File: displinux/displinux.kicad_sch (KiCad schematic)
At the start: 168 parts, among them J10 USB4105-GF-A, J11 Conn_02x03_Odd_Even, J12 Conn_02x17_Odd_Even, J13 Conn_01x02, J15 HR911105A, J2 AudioJack4, J3 AudioJack4, J4 USB4105-GF-A, J5 Conn_01x04, J6 Conn_01x06, J7 Conn_01x40_MountingPin, J8 Conn_01x24_MountingPin, J9 Conn_01x03, U1 SY8089AAAC, U2 SY8089AAAC, U3 SY8089AAAC, U4 SY7201ABC, U5 F133, U6 XC6206PxxxMR, U7 W25N01KV, U8 DP83848C, X1 ASE-50MHz, Y1 24M, Y2 Crystal

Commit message: add schematic
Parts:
- removed C12, C34, C6: 10u, Capacitor_SMD:C_0603_1608Metric, symbol Device:C
- removed C16, C17, C18, C19, C20, C21, C22, C24, C25, C26, C27, C32, C33, C35, C37, C39, C9: 0.1u, Capacitor_SMD:C_0603_1608Metric, symbol Device:C
- removed C28: 33p, Capacitor_SMD:C_0603_1608Metric, symbol Device:C
- removed D10, D11, D12, D13, D4, D6, D7, D8, D9: ESD9B3.3ST5G, Diode_SMD:D_SOD-923, symbol Diode:ESD9B3.3ST5G
- removed D3: D, Diode_SMD:D_SOD-323, symbol Device:D
- removed H5: MountingHole_Pad, Connector_Wire:SolderWirePad_1x01_SMD_5x10mm, symbol Mechanical:MountingHole_Pad
- removed J11: Conn_02x03_Odd_Even, Connector_PinHeader_2.00mm:PinHeader_2x03_P2.00mm_Vertical, symbol Connector_Generic:Conn_02x03_Odd_Even
- removed J13: Conn_01x02, Connector_PinHeader_2.00mm:PinHeader_1x02_P2.00mm_Vertical, symbol Connector_Generic:Conn_01x02
- removed J3: AudioJack4, Connector_Audio:Jack_3.5mm_PJ320D_Horizontal, symbol XassetteAsterisk-rescue:AudioJack4-Connector
- removed J5: Conn_01x04, Connector_PinSocket_2.00mm:PinSocket_1x04_P2.00mm_Vertical, symbol Connector_Generic:Conn_01x04
- removed JP1, JP2, JP3: Jumper_3_Open, Jumper:SolderJumper-3_P2.0mm_Open_TrianglePad1.0x1.5mm, symbol XassetteAsterisk-rescue:Jumper_3_Open-Jumper
- removed L3: 2.2u, Inductor_SMD:L_Wuerth_MAPI-2510, symbol Device:L
- removed R15, R4: 100k, Resistor_SMD:R_0603_1608Metric, symbol Device:R
- removed R19: 10M, Resistor_SMD:R_0603_1608Metric, symbol Device:R
- removed R28, R29: 10k, Resistor_SMD:R_0603_1608Metric, symbol Device:R
- removed R7: 200k, Resistor_SMD:R_0603_1608Metric, symbol Device:R
- removed RN1, RN2: R_Pack04, Resistor_SMD:R_Array_Convex_4x0603, symbol Device:R_Pack04
- removed U2: SY8089AAAC, Package_TO_SOT_SMD:SOT-23-5, symbol XassetteAsterisk-rescue:SY8089AAAC-2021-10-05_14-05-45
- removed U7: W25N01KV, Package_SON:WSON-8-1EP_6x5mm_P1.27mm_EP3.4x4.3mm, symbol XassetteAsterisk-rescue:W25Q32JVSS-Memory_Flash
- added C42: 10u, Capacitor_SMD:C_0603_1608Metric, symbol Device:C
- added C43, C46, C51, C52, C55, C57, C58, C60, C61, C62, C63: 0.1u, Capacitor_SMD:C_0603_1608Metric, symbol Device:C
- added D2: LED, LED_SMD:LED_0603_1608Metric, symbol Device:LED
- added R38: 1k, Resistor_SMD:R_0603_1608Metric, symbol Device:R
- added R42, R43, R44: 2.2K, Resistor_SMD:R_0603_1608Metric, symbol Device:R
- added R45: 100k, Resistor_SMD:R_0603_1608Metric, symbol Device:R
- added R49, R50, R51, R52, R53, R54: 10k, Resistor_SMD:R_0603_1608Metric, symbol Device:R
- added U6: XC6206P_1_2_MR, Package_TO_SOT_SMD:SOT-23, symbol Regulator_Linear:XC6206PxxxMR
- added U8: W25N01KV, Package_SON:WSON-8-1EP_6x5mm_P1.27mm_EP3.4x4.3mm, symbol XassetteAsterisk-rescue:W25Q32JVSS-Memory_Flash
- C11: renamed from C63; footprint Capacitor_SMD:C_0805_2012Metric -> Capacitor_SMD:C_0603_1608Metric
- C20: renamed from C61; footprint Capacitor_SMD:C_0805_2012Metric -> Capacitor_SMD:C_0603_1608Metric
- C21: renamed from C62; footprint Capacitor_SMD:C_0805_2012Metric -> Capacitor_SMD:C_0603_1608Metric
- C22: renamed from C64; footprint Capacitor_SMD:C_0805_2012Metric -> Capacitor_SMD:C_0603_1608Metric
- C24: renamed from C67; footprint Capacitor_SMD:C_0805_2012Metric -> Capacitor_SMD:C_0603_1608Metric
- C25: renamed from C69; footprint Capacitor_SMD:C_0805_2012Metric -> Capacitor_SMD:C_0603_1608Metric
- C26: renamed from C70; footprint Capacitor_SMD:C_0805_2012Metric -> Capacitor_SMD:C_0603_1608Metric
- C47, C48: value 1u -> 0.1u
- C8: renamed from C66; footprint Capacitor_SMD:C_0805_2012Metric -> Capacitor_SMD:C_0603_1608Metric
- C9: renamed from C68; footprint Capacitor_SMD:C_0805_2012Metric -> Capacitor_SMD:C_0603_1608Metric
- J1: renamed from J4; footprint USB4105-GF-A:GCT_USB4105-GF-A -> Connector_USB:USB_C_Receptacle_G-Switch_GT-USB-7010ASV
- J2: renamed from J10; footprint USB4105-GF-A:GCT_USB4105-GF-A -> Connector_USB:USB_C_Receptacle_G-Switch_GT-USB-7010ASV
- L1: renamed from L2; footprint Inductor_SMD:L_Wuerth_MAPI-2510 -> Inductor_SMD_Wurth:L_Wurth_WE-LQSH-3012
- L2: renamed from L4; footprint Inductor_SMD:L_Wuerth_MAPI-2510 -> Inductor_SMD_Wurth:L_Wurth_WE-LQSH-3012
- L3: renamed from L1; footprint Inductor_SMD:L_Wuerth_MAPI-2510 -> Inductor_SMD_Wurth:L_Wurth_WE-LQSH-3012
- R13: renamed from R43; footprint Resistor_SMD:R_0805_2012Metric -> Resistor_SMD:R_0603_1608Metric
- R14: renamed from R44; footprint Resistor_SMD:R_0805_2012Metric -> Resistor_SMD:R_0603_1608Metric
- R15: renamed from R45; footprint Resistor_SMD:R_0805_2012Metric -> Resistor_SMD:R_0603_1608Metric
- R16: renamed from R46; footprint Resistor_SMD:R_0805_2012Metric -> Resistor_SMD:R_0603_1608Metric
- R18: value 2.2k -> 7.87k
- R19: renamed from R50; footprint Resistor_SMD:R_0805_2012Metric -> Resistor_SMD:R_0603_1608Metric
- R20: renamed from R38; footprint Resistor_SMD:R_0805_2012Metric -> Resistor_SMD:R_0603_1608Metric
- R21: renamed from R51; footprint Resistor_SMD:R_0805_2012Metric -> Resistor_SMD:R_0603_1608Metric
- R22: renamed from R35; footprint Resistor_SMD:R_0805_2012Metric -> Resistor_SMD:R_0603_1608Metric
- R23: renamed from R36; footprint Resistor_SMD:R_0805_2012Metric -> Resistor_SMD:R_0603_1608Metric
- R24: renamed from R40; footprint Resistor_SMD:R_0805_2012Metric -> Resistor_SMD:R_0603_1608Metric
- R26: renamed from R47; footprint Resistor_SMD:R_0805_2012Metric -> Resistor_SMD:R_0603_1608Metric
- R27: renamed from R39; footprint Resistor_SMD:R_0805_2012Metric -> Resistor_SMD:R_0603_1608Metric
- R28: renamed from R48; footprint Resistor_SMD:R_0805_2012Metric -> Resistor_SMD:R_0603_1608Metric
- R29: renamed from R49; footprint Resistor_SMD:R_0805_2012Metric -> Resistor_SMD:R_0603_1608Metric
- R32: renamed from R34; footprint Resistor_SMD:R_0805_2012Metric -> Resistor_SMD:R_0603_1608Metric
- U5: renamed from U6; value XC6206PxxxMR -> XC6206P_2_8_MR
- XS1: footprint usd:Conn_uSDcard -> Connector_Card:microSD_HC_Hirose_DM3AT-SF-PEJM5
- renumbered C52 to C1, C60 to C10, C43 to C12, C38 to C15, C11 to C16, C5 to C17, C8 to C18, C54 to C19, C58 to C2, C65 to C23, C55 to C27, C29 to C28, C3 to C29, C14 to C3, C23 to C30, C30 to C31, C13 to C32, C31 to C33, C7 to C34, C10 to C35, C53 to C36, C36 to C37, C46 to C38, C51 to C39, C44 to C4, C42 to C41, C57 to C44, C2 to C45, C41 to C5, C1 to C53, C4 to C54, C45 to C6, C15 to C7, D2 to D1, D5 to D3, D1 to D5, J2 to J3, J12 to J4, J15 to J5, J8 to J6, J6 to J7, J7 to J8, R21 to R1, R13 to R10, R17 to R11, R11 to R12, R14 to R17, R23 to R2, R1 to R25, R26 to R3, R3 to R30, R6 to R31, R22 to R33, R2 to R34, R31 to R35, R32 to R36, R5 to R39, R27 to R4, R8 to R40, R20 to R41, R9 to R46, R24 to R47, R25 to R48, R30 to R5, R33 to R6, R12 to R7, R16 to R8, R10 to R9, U8 to U1, U1 to U2, U5 to U3, U3 to U4, U4 to U7
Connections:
- net VCC_PD is gone; now on net +3V3: C36.2, U3.66 (VCC-PD)
- net VCC_PG is gone; now on net +3V3: C12.2, U3.128 (VCC-PG)
- net +1V8: now also C40.1, C59.1, U3.28 (LDOA-OUT), C57.1, C58.1, C60.1, C61.1, C62.1, C63.1; no longer R18.1
- net +3V3: now also C50.1, J4.4 (Pin_4), J6.11 (Pin_11), U3.34 (VCC-PE), C42.2, C51.1, C52.1, C55.1, R42.1, R43.1, R44.1, R45.1, R49.1, U6.3 (VI), U8.8 (VCC); no longer C40.1, C56.1
- net +5V: now also J4.3 (Pin_3), R18.1
- net CLKO: now also J4.23 (Pin_23); no longer J4.33 (Pin_33)
- net CSI-PWDN: now also J6.8 (Pin_8), R38.1; no longer J6.5 (Pin_5)
- net CSI-RST#: now also J6.6 (Pin_6); no longer J6.4 (Pin_4)
- net GND: now also C49.2, C50.2, J4.31 (Pin_31), J4.32 (Pin_32), J4.33 (Pin_33), J4.34 (Pin_34), J6.15 (Pin_15), J6.2 (Pin_2), C42.1, C43.2, C46.2, C51.2, C52.2, C55.2, C57.2, C58.2, C60.2, C61.2, C62.2, C63.2, D2.1 (K), R38.2, R49.2, R50.2, R51.2, R52.2, R53.2, R54.2, U6.1 (GND), U8.4 (GND); no longer J4.13 (Pin_13), J4.14 (Pin_14), J6.1 (Pin_1), J6.11 (Pin_11), J6.14 (Pin_14)
- net HPOUTFB: now also J4.7 (Pin_7)
- net HS_MIC: no longer R18.2
- net LCD0-D0: now also J8.21 (Pin_21), R53.1; no longer J8.5 (Pin_5)
- net LCD0-D1: now also J8.22 (Pin_22), R54.1; no longer J8.6 (Pin_6)
- net LCD0-D16: now also J8.5 (Pin_5); no longer J8.21 (Pin_21)
- net LCD0-D17: now also J8.6 (Pin_6), R50.1; no longer J8.22 (Pin_22)
- net LCD0-D18: now also J8.7 (Pin_7); no longer J8.23 (Pin_23)
- net LCD0-D19: now also J8.8 (Pin_8); no longer J8.24 (Pin_24)
- net LCD0-D2: now also J8.23 (Pin_23); no longer J8.7 (Pin_7)
- net LCD0-D20: now also J8.9 (Pin_9); no longer J8.25 (Pin_25)
- net LCD0-D21: now also J8.10 (Pin_10); no longer J8.26 (Pin_26)
- net LCD0-D22: now also J8.11 (Pin_11); no longer J8.27 (Pin_27)
- net LCD0-D23: now also J8.12 (Pin_12); no longer J8.28 (Pin_28)
- net LCD0-D3: now also J8.24 (Pin_24); no longer J8.8 (Pin_8)
- net LCD0-D4: now also J8.25 (Pin_25); no longer J8.9 (Pin_9)
- net LCD0-D5: now also J8.26 (Pin_26); no longer J8.10 (Pin_10)
- net LCD0-D6: now also J8.27 (Pin_27); no longer J8.11 (Pin_11)
- net LCD0-D7: now also J8.28 (Pin_28); no longer J8.12 (Pin_12)
- net LCD0-D8: now also R51.1
- net LCD0-D9: now also R52.1
- net MIC3N: now also J4.8 (Pin_8)
- net MIC3P: now also J4.10 (Pin_10)
- net NCSI0-D0: now also J6.19 (Pin_19); no longer J6.22 (Pin_22)
- net NCSI0-D2: now also J6.22 (Pin_22); no longer J6.20 (Pin_20)
- net NCSI0-D3: now also J6.20 (Pin_20); no longer J6.19 (Pin_19)
- net NCSI0-D5: now also J6.16 (Pin_16); no longer J6.17 (Pin_17)
- net NCSI0-D6: now also J6.14 (Pin_14); no longer J6.16 (Pin_16)
- net NCSI0-D7: now also J6.12 (Pin_12); no longer J6.15 (Pin_15)
- net NCSI0-HSYNC: now also J6.9 (Pin_9)
- net NCSI0-MCLK: now also J6.13 (Pin_13)
- net NCSI0-PCLK: now also J6.17 (Pin_17)
- net NCSI0-VSYNC: now also J6.7 (Pin_7)
- net PG13: now also J4.21 (Pin_21); no longer J4.10 (Pin_10)
- net RST: now also C56.1, R45.2
- net TP_X2: now also J7.4 (Pin_4); no longer J7.3 (Pin_3)
- net TP_Y1: now also J7.3 (Pin_3); no longer J7.4 (Pin_4)
- net TWI2-SCK: now also J6.5 (Pin_5); no longer J6.3 (Pin_3)
- net TWI2-SDA: now also J6.3 (Pin_3); no longer J6.2 (Pin_2)
- net VDD-CORE: now also C47.1, C48.1, C49.1, C46.1
- net at U3.111 (TVIN-VRN): no longer C47.1
- net at U3.110 (TVIN-VRP): no longer C48.1
- net SPI0_HOLD: now reaches J4.25 (Pin_25)
- net SPI0_HOLD: now also U3.14 (PC7), U8.7 (IO3)
- net SPI0_WP: now reaches J4.26 (Pin_26)
- net SPI0_WP: now also U3.15 (PC6), U8.3 (IO2)
- net SPI0_MISO: now reaches J4.27 (Pin_27)
- net SPI0_MISO: now also FEL1.2 (B), R11.1, R8.2, U3.16 (PC5), U8.2 (DO(IO1))
- removed net CSI-AVDD: C59.1, J6.10 (Pin_10), J6.9 (Pin_9), U3.28 (LDOA-OUT)
- net CSI-DVDD renamed CSI-DVDD-2_8V
- net CSI-DVDD-2_8V: now also J6.4 (Pin_4); no longer J6.8 (Pin_8)
- removed net CSI-IOVDD: J6.23 (Pin_23), J6.24 (Pin_24), U3.34 (VCC-PE)
- net FMINL: no longer names the net of U3.94 (FMINL)
- net FMINR: no longer names the net of U3.93 (FMINR)
- net LINEL: no longer names the net of U3.96 (LINEINL)
- net LINEL: no longer C49.2
- net LINER: no longer names the net of U3.95 (LINEINR)
- net LINER: no longer C50.2
- net PC2 renamed SPI0_CLK
- net SPI0_CLK: now also J4.30 (Pin_30), U8.6 (CLK); no longer J4.28 (Pin_28)
- net PC3 renamed SPI0_CS0
- net SPI0_CS0: now also R44.2, U8.1 (~{CS})
- net PC4 renamed SPI0_MOSI
- net SPI0_MOSI: now also J4.28 (Pin_28), U8.5 (DI(IO0)); no longer J4.30 (Pin_30)
- removed net PC5: FEL1.2 (B), J4.31 (Pin_31), R11.1, R8.2, U3.16 (PC5)
- removed net PC6: J4.32 (Pin_32), U3.15 (PC6)
- removed net PC7: J4.34 (Pin_34), U3.14 (PC7)
- net PF0 renamed SDC0-D1
- net PF1 renamed SDC0-D0
- net PF2 renamed SDC0-CLK
- net PF3 renamed SDC0-CMD
- net SDC0-CMD: now also R42.2
- net PF4 renamed SDC0-D3
- net PF5 renamed SDC0-D2
- net PF6 renamed SDC0-CD
- net SDC0-CD: now also R43.2
- net TVIN0: no longer names the net of U3.108 (TVIN0)
- net TVIN1: no longer names the net of U3.109 (TVIN1)
- net TVOUT: no longer names the net of U3.78 (TVOUT0)
- new net: D2.2 (A), R18.2
- new net CSI-DVDD-1_2V: C43.1, J6.10 (Pin_10), U6.2 (VO)
- no-connect marks 20 -> 19
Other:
- note added: "BOOT"
- note added: "CAMERA"
- note added: "LCD-RGB"
- note added: "UART0"
- note removed: "Camera"
- note removed: "IO Port voltage selection"
- note removed: "JUMPERS"
- note removed: "LCD"
- note removed: "Leave unconnected if board is powered by 5V"
- note removed: "Leave unconnected if headphone is not used"
- note removed: "Leave unconnected if line-in is not used"
- moved on the sheet: C16, C17, C18, C28, C29, C3, C30, C31, C32, C33, C34, C35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

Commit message: start tracing
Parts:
- removed J4: Conn_02x17_Odd_Even, Connector_PinSocket_2.54mm:PinSocket_2x17_P2.54mm_Vertical, symbol Connector_Generic:Conn_02x17_Odd_Even
- removed J9: Conn_01x03, Connector_PinHeader_2.54mm:PinHeader_1x03_P2.54mm_Vertical, symbol Connector_Generic:Conn_01x03
- added J10: Conn_01x03, Connector_PinHeader_2.54mm:PinHeader_1x03_P2.54mm_Vertical, symbol Connector_Generic:Conn_01x03
- added J4: Conn_02x10_Counter_Clockwise, Connector_PinHeader_2.54mm:PinHeader_2x10_P2.54mm_Vertical, symbol Connector_Generic:Conn_02x10_Counter_Clockwise
- added J9: Conn_01x02_Pin, Connector_PinHeader_2.54mm:PinHeader_1x02_P2.54mm_Vertical, symbol Connector:Conn_01x02_Pin
- C10: footprint Capacitor_SMD:C_0805_2012Metric -> Capacitor_SMD:C_0603_1608Metric
- D3, D5: footprint Diode_SMD:D_SOD-323 -> Diode_SMD:D_SOD-523
- J5: footprint Connector_RJ:RJ45_Wuerth_7499111446_Horizontal -> Connector_RJ:RJ45_Hanrun_HR911105A_Horizontal
- J7: footprint Connector_PinHeader_2.00mm:PinHeader_1x06_P2.00mm_Vertical -> Connector_PinHeader_2.54mm:PinHeader_1x06_P2.54mm_Vertical
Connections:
- net +3V3: now also R24.1, J4.2 (Pin_2); no longer R49.1
- net +5V: now also J4.1 (Pin_1)
- net CLKO: now also J4.17 (Pin_17)
- net GND: now also J10.1 (Pin_1), J4.18 (Pin_18), J4.19 (Pin_19), J4.20 (Pin_20)
- net LCD0-D16: now also R49.1
- net MIC3N: now also J10.3 (Pin_3)
- net MIC3P: now also J10.2 (Pin_2)
- net NCSI0-MCLK: now also J9.2 (Pin_2)
- net NCSI0-PCLK: now also J9.1 (Pin_1)
- net PG10: now also J4.7 (Pin_7)
- net PG11: now also J4.8 (Pin_8)
- net PG6: now also J4.3 (Pin_3)
- net PG7: now also J4.4 (Pin_4)
- net PG8: now also J4.5 (Pin_5)
- net PG9: now also J4.6 (Pin_6)
- net SPI0_CLK: now also J4.14 (Pin_14)
- net SPI0_CS0: now also J4.13 (Pin_13)
- net SPI0_HOLD: now also J4.9 (Pin_9)
- net SPI0_MISO: now also J4.11 (Pin_11)
- net SPI0_MOSI: now also J4.12 (Pin_12)
- net SPI0_WP: now also J4.10 (Pin_10)
- net TWI2-SCK: now also J4.16 (Pin_16)
- net TWI2-SDA: now also J4.15 (Pin_15)
- net at R20.1, U1.39 (RX_DV/MII_MODE): no longer R24.1
- net PG13: no longer names the net of U3.125 (PG13)
- no-connect marks 19 -> 33
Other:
- moved on the sheet: R20, R22, R23, R24

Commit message: tracing finished Need to check
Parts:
- D5: footprint Diode_SMD:D_SOD-523 -> Diode_SMD:D_0805_2012Metric
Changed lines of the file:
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@@
 			)
 		)
-		(property "Footprint" "Diode_SMD:D_SOD-523"
+		(property "Footprint" "Diode_SMD:D_0805_2012Metric"
 			(at 548.64 313.69 0)
 			(effects

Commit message: add fixes
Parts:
- removed R33: 0, Resistor_SMD:R_0603_1608Metric, symbol Device:R
- removed R47, R48: 10k, Resistor_SMD:R_0603_1608Metric, symbol Device:R
- added C13: 10u, Capacitor_SMD:C_0603_1608Metric, symbol Device:C
- C40, C44: value 0.1u -> 10u
- D5: footprint Diode_SMD:D_0805_2012Metric -> Diode_SMD:D_2010_5025Metric
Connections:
- net DISP is gone; now on net +3V3: J8.31 (Pin_31)
- net GND: now also U3.91 (AGND), C13.2
- net LDOB-OUT: now also C13.1
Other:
- note added: "LCD-MIPI"
- note added: "closer to pin 49"
- note removed: "Choose pull-up / pull-down according to LCD spec or leave unconnected when LCD is not used"
- moved on the sheet: J9

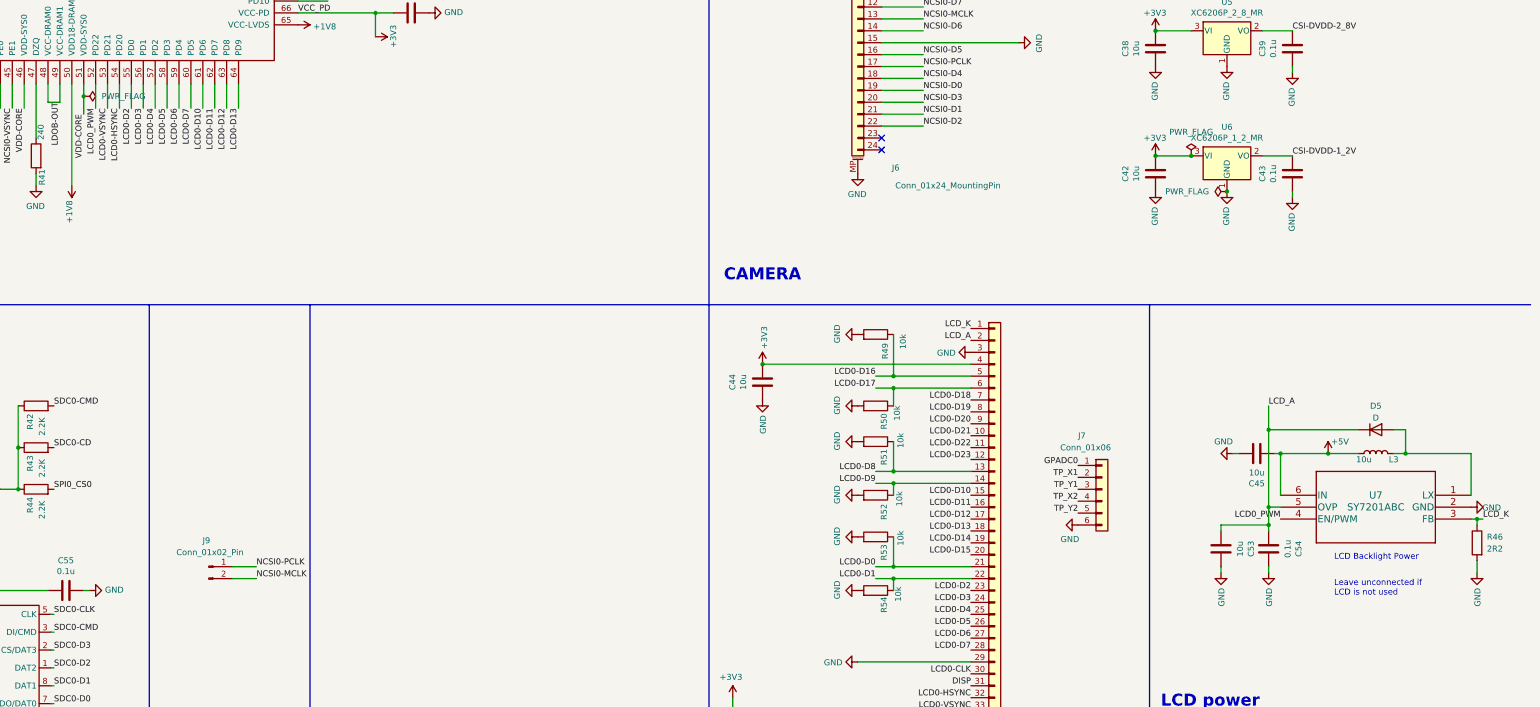
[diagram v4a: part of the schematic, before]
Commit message: fix display power
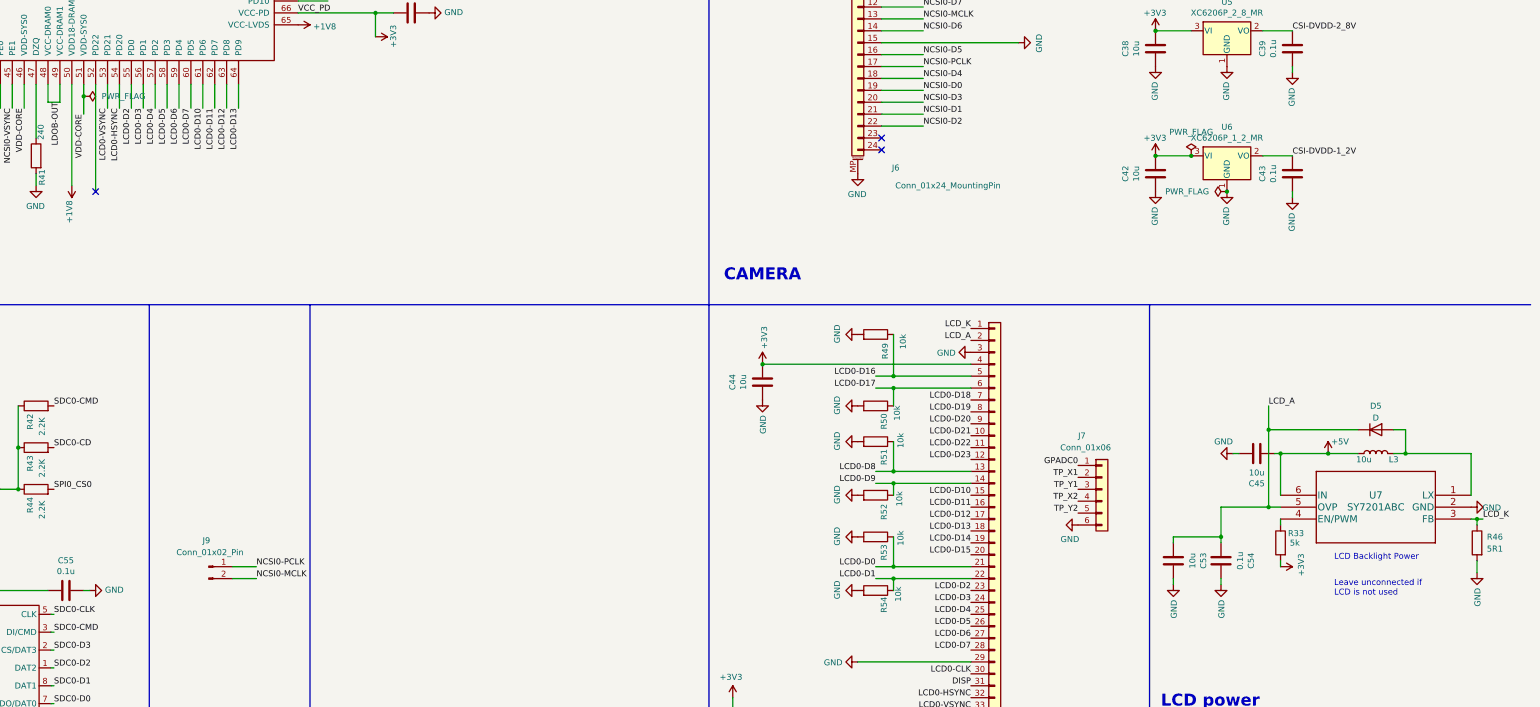
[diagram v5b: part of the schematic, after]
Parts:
- added R33: 5k, Resistor_SMD:R_0603_1608Metric, symbol Device:R
- R46: value 2R2 -> 5R1
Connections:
- net +3V3: now also R33.2
- net LCD0_PWM: no longer names the net of U3.52 (PD22)
- net LCD0_PWM: no longer U7.4 (EN/PWM)
- new net: R33.1, U7.4 (EN/PWM)
- no-connect marks 33 -> 34
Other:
- moved on the sheet: C53, C54
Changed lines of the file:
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@@
 	)
 	(junction
-		(at 525.78 334.01)
+		(at 515.62 336.55)
 		(diameter 0)
 		(color 0 0 0 0)
@@
 	)
 	(no_connect
+		(at 275.59 262.89)
+	)
+	(no_connect
 		(at 457.2 97.79)
 	)
@@
 	(wire
 		(pts
-			(xy 525.78 330.2) (xy 525.78 334.01)
+			(xy 515.62 330.2) (xy 515.62 336.55)
 		)
 		(stroke
@@
 	(wire
 		(pts
+			(xy 528.32 332.74) (xy 528.32 334.01)
+		)
+		(stroke
+			(width 0)
+			(type default)
+		)
+	)
+	(wire
+		(pts
 			(xy 495.3 21.59) (xy 496.57 21.59)
 		)
@@
 	(wire
 		(pts
-			(xy 515.62 334.01) (xy 515.62 335.28)
+			(xy 505.46 336.55) (xy 505.46 337.82)
 		)
 		(stroke
@@
 	(wire
 		(pts
-			(xy 275.59 245.11) (xy 275.59 240.03)
-		)
-		(stroke
-			(width 0)
-			(type default)
-		)
-	)
-	(wire
-		(pts
 			(xy 570.23 332.74) (xy 571.5 332.74)
 		)
@@
 	(wire
 		(pts
-			(xy 525.78 334.01) (xy 525.78 335.28)
+			(xy 515.62 336.55) (xy 515.62 337.82)
 		)
 		(stroke
@@
 	(wire
 		(pts
-			(xy 525.78 334.01) (xy 515.62 334.01)
+			(xy 515.62 336.55) (xy 505.46 336.55)
 		)
 		(stroke
@@
 	(wire
 		(pts
-			(xy 515.62 344.17) (xy 515.62 342.9)
+			(xy 505.46 346.71) (xy 505.46 345.44)
 		)
 		(stroke
@@
 	(wire
 		(pts
+			(xy 515.62 330.2) (xy 525.78 330.2)
+		)
+		(stroke
+			(width 0)
+			(type default)
+		)
+	)
+	(wire
+		(pts
 			(xy 162.56 245.11) (xy 171.45 245.11)
 		)
@@
 	(wire
 		(pts
-			(xy 525.78 344.17) (xy 525.78 342.9)
+			(xy 515.62 346.71) (xy 515.62 345.44)
 		)
 		(stroke
@@
 	(wire
 		(pts
+			(xy 275.59 240.03) (xy 275.59 262.89)
+		)
+		(stroke
+			(width 0)
+			(type default)
+		)
+	)
+	(wire
+		(pts
 			(xy 518.16 318.77) (xy 519.43 318.77)
 		)
@@
 	(wire
 		(pts
+			(xy 528.32 341.63) (xy 528.32 342.9)
+		)
+		(stroke
+			(width 0)
+			(type default)
+		)
+	)
+	(wire
+		(pts
 			(xy 547.37 146.05) (xy 554.99 146.05)
 		)
@@
 		)
 	)
-	(label "LCD0_PWM"
-		(at 275.59 245.11 270)
-		(fields_autoplaced yes)
-		(effects
-			(font
-				(size 1.27 1.27)
-			)
-			(justify right bottom)
-		)
-	)
 	(label "SPI0_MISO"
 		(at 207.01 186.69 180)
@@
 		)
 	)
-	(label "LCD0_PWM"
-		(at 528.32 332.74 180)
-		(fields_autoplaced yes)
-		(effects
-			(font
-				(size 1.27 1.27)
-			)
-			(justify right bottom)
-		)
-	)
 	(label "NCSI0-D4"
 		(at 452.12 238.76 0)
@@
 	(symbol
 		(lib_id "XassetteAsterisk-rescue:GND-power")
-		(at 515.62 344.17 0)
+		(at 505.46 346.71 0)
 		(unit 1)
 		(exclude_from_sim no)
@@
 		(dnp no)
 		(property "Reference" "#PWR0129"
-			(at 515.62 350.52 0)
+			(at 505.46 353.06 0)
 			(effects
 				(font
@@
 		)
 		(property "Value" "GND"
-			(at 515.747 347.4212 90)
+			(at 505.587 349.9612 90)
 			(effects
 				(font
@@
 		)
 		(property "Footprint" ""
-			(at 515.62 344.17 0)
+			(at 505.46 346.71 0)
 			(effects
 				(font
@@
 		)
 		(property "Datasheet" ""
-			(at 515.62 344.17 0)
+			(at 505.46 346.71 0)
 			(effects
 				(font
@@
 		)
 		(property "Description" ""
-			(at 515.62 344.17 0)
+			(at 505.46 346.71 0)
 			(effects
 				(font
@@
 	(symbol
 		(lib_id "Device:C")
-		(at 515.62 339.09 0)
+		(at 505.46 341.63 0)
 		(mirror y)
 		(unit 1)
@@
 		(dnp no)
 		(property "Reference" "C53"
-			(at 522.0208 339.09 90)
+			(at 511.8608 341.63 90)
 			(effects
 				(font
@@
 		)
 		(property "Value" "10u"
-			(at 519.7094 339.09 90)
+			(at 509.5494 341.63 90)
 			(effects
 				(font
@@
 		)
 		(property "Footprint" "Capacitor_SMD:C_0603_1608Metric"
-			(at 514.6548 342.9 0)
+			(at 504.4948 345.44 0)
 			(effects
 				(font
@@
 		)
 		(property "Datasheet" "~"
-			(at 515.62 339.09 0)
+			(at 505.46 341.63 0)
 			(effects
 				(font
@@
 		)
 		(property "Description" ""
-			(at 515.62 339.09 0)
+			(at 505.46 341.63 0)
 			(effects
 				(font
@@
 			)
 		)
-		(property "Value" "2R2"
+		(property "Value" "5R1"
 			(at 574.04 339.09 0)
 			(effects
@@
 	(symbol
 		(lib_id "XassetteAsterisk-rescue:GND-power")
-		(at 525.78 344.17 0)
+		(at 515.62 346.71 0)
 		(unit 1)
 		(exclude_from_sim no)
@@
 		(dnp no)
 		(property "Reference" "#PWR0130"
-			(at 525.78 350.52 0)
+			(at 515.62 353.06 0)
 			(effects
 				(font
@@
 		)
 		(property "Value" "GND"
-			(at 525.907 347.4212 90)
+			(at 515.747 349.9612 90)
 			(effects
 				(font
@@
 		)
 		(property "Footprint" ""
-			(at 525.78 344.17 0)
+			(at 515.62 346.71 0)
 			(effects
 				(font
@@
 		)
 		(property "Datasheet" ""
-			(at 525.78 344.17 0)
+			(at 515.62 346.71 0)
 			(effects
 				(font
@@
 		)
 		(property "Description" ""
-			(at 525.78 344.17 0)
+			(at 515.62 346.71 0)
 			(effects
 				(font
@@
 	)
 	(symbol
+		(lib_id "XassetteAsterisk-rescue:+3V3-power")
+		(at 528.32 342.9 270)
+		(mirror x)
+		(unit 1)
+		(exclude_from_sim no)
+		(in_bom yes)
+		(on_board yes)
+		(dnp no)
+		(property "Reference" "#PWR048"
+			(at 524.51 342.9 0)
+			(effects
+				(font
+					(size 1.27 1.27)
+				)
+				(hide yes)
+			)
+		)
+		(property "Value" "+3V3"
+			(at 532.7142 342.519 0)
+			(effects
+				(font
+					(size 1.27 1.27)
+				)
+			)
+		)
+		(property "Footprint" ""
+			(at 528.32 342.9 0)
+			(effects
+				(font
+					(size 1.27 1.27)
+				)
+				(hide yes)
+			)
+		)
+		(property "Datasheet" ""
+			(at 528.32 342.9 0)
+			(effects
+				(font
+					(size 1.27 1.27)
+				)
+				(hide yes)
+			)
+		)
+		(property "Description" ""
+			(at 528.32 342.9 0)
+			(effects
+				(font
+					(size 1.27 1.27)
+				)
+				(hide yes)
+			)
+		)
+		(pin "1"
+		)
+		(instances
+			(project "displinux"
+				(path "/c097ddf1-c967-4eca-a041-b7e2441e5d19"
+					(reference "#PWR048")
+					(unit 1)
+				)
+			)
+		)
+	)
+	(symbol
 		(lib_id "XassetteAsterisk-rescue:+1V8-power")
 		(at 280.67 135.89 0)
@@
 	(symbol
 		(lib_id "Device:C")
-		(at 525.78 339.09 0)
+		(at 515.62 341.63 0)
 		(mirror y)
 		(unit 1)
@@
 		(dnp no)
 		(property "Reference" "C54"
-			(at 532.1808 339.09 90)
+			(at 522.0208 341.63 90)
 			(effects
 				(font
@@
 		)
 		(property "Value" "0.1u"
-			(at 529.8694 339.09 90)
+			(at 519.7094 341.63 90)
 			(effects
 				(font
@@
 		)
 		(property "Footprint" "Capacitor_SMD:C_0603_1608Metric"
-			(at 524.8148 342.9 0)
+			(at 514.6548 345.44 0)
 			(effects
 				(font
@@
 		)
 		(property "Datasheet" "~"
-			(at 525.78 339.09 0)
+			(at 515.62 341.63 0)
 			(effects
 				(font
@@
 		)
 		(property "Description" ""
-			(at 525.78 339.09 0)
+			(at 515.62 341.63 0)
 			(effects
 				(font
@@
 					(unit 1)
 				)
+			)
+		)
+	)
+	(symbol
+		(lib_id "Device:R")
+		(at 528.32 337.82 0)
+		(mirror y)
+		(unit 1)
+		(exclude_from_sim no)
+		(in_bom yes)
+		(on_board yes)
+		(dnp no)
+		(property "Reference" "R33"
+			(at 531.622 335.788 0)
+			(effects
+				(font
+					(size 1.27 1.27)
+				)
+			)
+		)
+		(property "Value" "5k"
+			(at 531.368 337.82 0)
+			(effects
+				(font
+					(size 1.27 1.27)
+				)
+			)
+		)
+		(property "Footprint" "Resistor_SMD:R_0603_1608Metric"
+			(at 530.098 337.82 90)
+			(effects
+				(font
+					(size 1.27 1.27)
+				)
+				(hide yes)
+			)
+		)
+		(property "Datasheet" "~"
+			(at 528.32 337.82 0)
+			(effects
+				(font
+					(size 1.27 1.27)
+				)
+				(hide yes)
+			)
+		)
+		(property "Description" ""
+			(at 528.32 337.82 0)
+			(effects
+				(font
+					(size 1.27 1.27)
+				)
+				(hide yes)
+			)
+		)
+		(pin "1"
+		)
+		(pin "2"
+		)
+		(instances
+			(project "displinux"
+				(path "/c097ddf1-c967-4eca-a041-b7e2441e5d19"
+					(reference "R33")
+					(unit 1)
+				)
